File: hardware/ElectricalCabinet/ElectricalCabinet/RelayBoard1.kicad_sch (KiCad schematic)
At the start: 0 parts

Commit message: Cabinet Schematics Update
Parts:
- added C1: 0.1uF, Capacitor_SMD:C_0805_2012Metric, symbol Device:C
- added D1, D2, D3, D4, D5, D6, D7, D8: LED, LED_SMD:LED_0805_2012Metric, symbol Device:LED
- added J1: Screw_Terminal_01x09, TerminalBlock:TerminalBlock_MaiXu_MX126-5.0-09P_1x09_P5.00mm, symbol Connector:Screw_Terminal_01x09
- added J2: Screw_Terminal_01x06, TerminalBlock:TerminalBlock_MaiXu_MX126-5.0-06P_1x06_P5.00mm, symbol Connector:Screw_Terminal_01x06
- added K1, K2, K3, K4, K5, K6, K7, K8: G3MB-202P DC5, TrafficLightLibrary:G3MB_202P_DC5, symbol TrafficLightLibrary:G3MB-202P_DC5
- added R1, R2, R3, R4, R5, R6, R7, R8: 1kΩ, Resistor_SMD:R_0805_2012Metric, symbol Device:R
- added U2: TPIC6B595N, TrafficLightLibrary:TPIC6B595N, symbol TrafficLightLibrary:TPIC6B595N
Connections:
- new net: C1.1, J2.2 (Pin_2), U2.10 (GND), U2.11 (GND), U2.19 (GND), U2.9 (~{G})
- new net: J2.4 (Pin_4), U2.12 (RCK)
- new net: J2.3 (Pin_3), U2.13 (SRCK)
- new net: K5.4, R5.2, U2.14 (DRAIN4)
- new net: K6.4, R6.2, U2.15 (DRAIN5)
- new net: K7.4, R7.2, U2.16 (DRAIN6)
- new net: K8.4, R8.2, U2.17 (DRAIN7)
- new net: J2.1 (Pin_1), U2.18 (SEROUT)
- new net: C1.2, J2.6 (Pin_6), U2.2 (VCC), U2.8 (~{SRCLR})
- new net: K1.4, R1.2, U2.4 (DRAIN0)
- new net: K2.4, R2.2, U2.5 (DRAIN1)
- new net: K3.4, R3.2, U2.6 (DRAIN2)
- new net: K4.4, R4.2, U2.7 (DRAIN3)
- new net: J1.5 (Pin_5), K5.2
- new net: D1.2 (A), D2.2 (A), D3.2 (A), D4.2 (A), D5.2 (A), D6.2 (A), D7.2 (A), D8.2 (A), K1.3, K2.3, K3.3, K4.3, K5.3, K6.3, K7.3, K8.3
- new net: J1.7 (Pin_7), K7.2
- new net: J1.4 (Pin_4), K4.2
- new net: D7.1 (K), R7.1
- new net: D8.1 (K), R8.1
- new net: D6.1 (K), R6.1
- new net: J1.3 (Pin_3), K3.2
- new net: D5.1 (K), R5.1
- new net: D3.1 (K), R3.1
- new net: D4.1 (K), R4.1
- new net: D1.1 (K), R1.1
- new net: J1.1 (Pin_1), K1.2
- new net: J1.2 (Pin_2), K2.2
- new net: J1.6 (Pin_6), K6.2
- new net: J1.8 (Pin_8), K8.2
- new net: D2.1 (K), R2.1
- new net 110vAC Hawt: J1.9 (Pin_9), K1.1, K2.1, K3.1, K4.1, K5.1, K6.1, K7.1, K8.1
- new net SERIN: J2.5 (Pin_5), U2.3 (SERIN)
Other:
- note added: "110vAC Hawt"

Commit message: More updates
Added drawing sheets, wire label scheme, signal list, and traffic light label image to docs folder
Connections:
- net 110vAC Hawt: no longer names the net of J1.9 (Pin_9), K1.1, K2.1, K3.1, K4.1, K5.1, K6.1, K7.1, K8.1
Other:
- note removed: "110vAC Hawt"
- moved on the sheet: C1, D1, D2, D3, D4, D5, D6, D7, D8, K1, K2, K3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

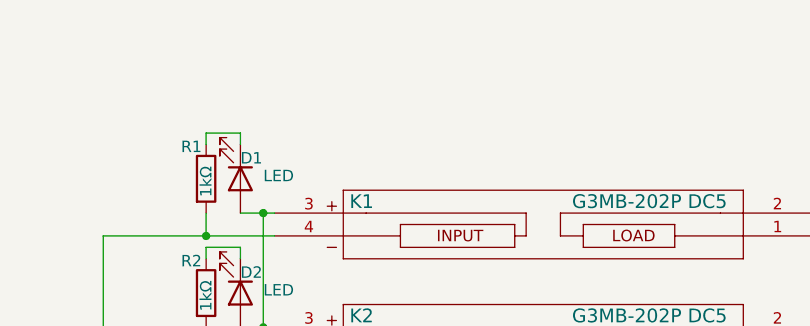
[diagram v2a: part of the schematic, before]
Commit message: Further wiring updates
Populated 6100 Bus
Corrected number of relay boards
Added 110v outputs to relay boards and noted light positon
Uploaded light scheme to documents folder
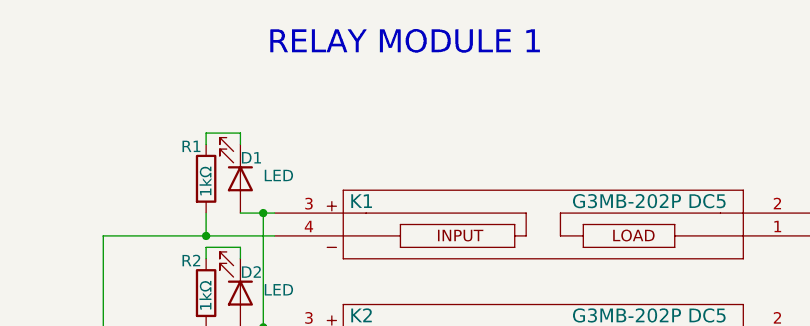
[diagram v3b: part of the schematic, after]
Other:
- note added: "RELAY MODULE 1"
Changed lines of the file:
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@@
 	(generator_version "10.0")
 	(paper "USLetter")
+	(text "RELAY MODULE 1"
+		(exclude_from_sim no)
+		(at 117.348 39.624 0)
+		(effects
+			(font
+				(size 2.54 2.54)
+			)
+		)
+	)
 	(junction
 		(at 165.1 149.86)
@@
 		(shape input)
 		(at 187.96 58.42 0)
-		(fields_autoplaced yes)
 		(effects
 			(font
@@
 			(justify left)
 		)
-		(property "Intersheetrefs" "${INTERSHEET_REFS}"
+		(property "Intersheetrefs" "LIGHTS"
 			(at 198.5651 58.42 0)
 			(hide yes)
@@
 			)
 		)
-		(property "A1" "Ref 312"
-			(at 187.96 62.2618 0)
-			(hide yes)
+		(property "REF" "A1"
+			(at 198.12 58.42 0)
 			(show_name no)
 			(do_not_autoplace no)
@@
 		(shape input)
 		(at 187.96 63.5 0)
-		(fields_autoplaced yes)
 		(effects
 			(font
@@
 			(justify left)
 		)
-		(property "Intersheetrefs" "${INTERSHEET_REFS}"
+		(property "Intersheetrefs" "LIGHTS"
 			(at 198.5651 63.5 0)
 			(hide yes)
+			(show_name no)
+			(do_not_autoplace no)
+			(effects
+				(font
+					(size 1.27 1.27)
+				)
+				(justify left)
+			)
+		)
+		(property "REF" "A3"
+			(at 198.12 63.5 0)
 			(show_name no)
 			(do_not_autoplace no)
@@
 		(shape input)
 		(at 187.96 73.66 0)
-		(fields_autoplaced yes)
 		(effects
 			(font
@@
 			(justify left)
 		)
-		(property "Intersheetrefs" "${INTERSHEET_REFS}"
+		(property "Intersheetrefs" "LIGHTS"
 			(at 198.5651 73.66 0)
 			(hide yes)
+			(show_name no)
+			(do_not_autoplace no)
+			(effects
+				(font
+					(size 1.27 1.27)
+				)
+				(justify left)
+			)
+		)
+		(property "REF" "B1"
+			(at 198.12 73.66 0)
 			(show_name no)
 			(do_not_autoplace no)
@@
 		(shape input)
 		(at 187.96 76.2 0)
-		(fields_autoplaced yes)
 		(effects
 			(font
@@
 			(justify left)
 		)
-		(property "Intersheetrefs" "${INTERSHEET_REFS}"
+		(property "Intersheetrefs" "LIGHTS"
 			(at 198.5651 76.2 0)
 			(hide yes)
+			(show_name no)
+			(do_not_autoplace no)
+			(effects
+				(font
+					(size 1.27 1.27)
+				)
+				(justify left)
+			)
+		)
+		(property "REF" "B2"
+			(at 198.12 76.2 0)
 			(show_name no)
 			(do_not_autoplace no)
@@
 		(shape input)
 		(at 187.96 66.04 0)
-		(fields_autoplaced yes)
 		(effects
 			(font
@@
 			(justify left)
 		)
-		(property "Intersheetrefs" "${INTERSHEET_REFS}"
+		(property "Intersheetrefs" "LIGHTS"
 			(at 198.5651 66.04 0)
 			(hide yes)
+			(show_name no)
+			(do_not_autoplace no)
+			(effects
+				(font
+					(size 1.27 1.27)
+				)
+				(justify left)
+			)
+		)
+		(property "REF" "A4"
+			(at 198.12 66.04 0)
 			(show_name no)
 			(do_not_autoplace no)
@@
 		(shape input)
 		(at 187.96 71.12 0)
-		(fields_autoplaced yes)
 		(effects
 			(font
@@
 			(justify left)
 		)
-		(property "Intersheetrefs" "${INTERSHEET_REFS}"
+		(property "Intersheetrefs" "LIGHTS"
 			(at 198.5651 71.12 0)
 			(hide yes)
+			(show_name no)
+			(do_not_autoplace no)
+			(effects
+				(font
+					(size 1.27 1.27)
+				)
+				(justify left)
+			)
+		)
+		(property "REF" "A6"
+			(at 198.12 71.12 0)
 			(show_name no)
 			(do_not_autoplace no)
@@
 		(shape input)
 		(at 187.96 60.96 0)
-		(fields_autoplaced yes)
 		(effects
 			(font
@@
 			(justify left)
 		)
-		(property "Intersheetrefs" "${INTERSHEET_REFS}"
+		(property "Intersheetrefs" "LIGHTS"
 			(at 198.5651 60.96 0)
 			(hide yes)
+			(show_name no)
+			(do_not_autoplace no)
+			(effects
+				(font
+					(size 1.27 1.27)
+				)
+				(justify left)
+			)
+		)
+		(property "REF" "A2"
+			(at 198.12 60.96 0)
 			(show_name no)
 			(do_not_autoplace no)
@@
 		(shape input)
 		(at 187.96 68.58 0)
-		(fields_autoplaced yes)
 		(effects
 			(font
@@
 			(justify left)
 		)
-		(property "Intersheetrefs" "${INTERSHEET_REFS}"
+		(property "Intersheetrefs" "LIGHTS"
 			(at 198.5651 68.58 0)
 			(hide yes)
+			(show_name no)
+			(do_not_autoplace no)
+			(effects
+				(font
+					(size 1.27 1.27)
+				)
+				(justify left)
+			)
+		)
+		(property "REF" "A5"
+			(at 198.12 68.58 0)
 			(show_name no)
 			(do_not_autoplace no)
@@
 			)
 		)
-		(property "Ref" "Ref 334"
+		(property "Ref" "Ref 434"
 			(at 26.67 147.32 0)
 			(show_name no)

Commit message: Electrical Cabinet done
Electrical Cabinet done, let me know if there are any changes or mistakes.
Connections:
- net SERIN is gone; now on net 7500-1: J2.5 (Pin_5), U2.3 (SERIN)
- net 5000-3: now also C1.1, J2.2 (Pin_2), U2.10 (GND), U2.11 (GND), U2.19 (GND), U2.9 (~{G})
- net 5500-3: now also C1.2, J2.6 (Pin_6), U2.2 (VCC), U2.8 (~{SRCLR})
- net 7500-2: now also J2.1 (Pin_1), U2.18 (SEROUT)
- net 8200-2: now also J2.4 (Pin_4), U2.12 (RCK)
- net 8300-2: now also J2.3 (Pin_3), U2.13 (SRCK)
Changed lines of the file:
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@@
+	)
+	(junction
+		(at 43.18 142.24)
+		(diameter 0)
+		(color 0 0 0 0)
+	)
+	(junction
+		(at 43.18 144.78)
+		(diameter 0)
+		(color 0 0 0 0)
 	)
 	(junction
@@
 	)
 	(junction
+		(at 43.18 137.16)
+		(diameter 0)
+		(color 0 0 0 0)
+	)
+	(junction
 		(at 67.31 125.73)
 		(diameter 0)
@@
 	)
 	(junction
+		(at 43.18 147.32)
+		(diameter 0)
+		(color 0 0 0 0)
+	)
+	(junction
 		(at 95.25 137.16)
 		(diameter 0)
@@
 	)
 	(junction
+		(at 43.18 139.7)
+		(diameter 0)
+		(color 0 0 0 0)
+	)
+	(junction
 		(at 101.6 147.32)
 		(diameter 0)
 		(color 0 0 0 0)
 	)
+	(junction
+		(at 43.18 134.62)
+		(diameter 0)
+		(color 0 0 0 0)
+	)
 	(wire
 		(pts
@@
 	(wire
 		(pts
+			(xy 36.83 134.62) (xy 43.18 134.62)
+		)
+		(stroke
+			(width 0)
+			(type default)
+		)
+	)
+	(wire
+		(pts
 			(xy 57.15 134.62) (xy 46.99 134.62)
 		)
@@
 	(wire
 		(pts
+			(xy 36.83 137.16) (xy 43.18 137.16)
+		)
+		(stroke
+			(width 0)
+			(type default)
+		)
+	)
+	(wire
+		(pts
 			(xy 165.1 149.86) (xy 162.56 149.86)
 		)
@@
 	(wire
 		(pts
+			(xy 36.83 147.32) (xy 43.18 147.32)
+		)
+		(stroke
+			(width 0)
+			(type default)
+		)
+	)
+	(wire
+		(pts
 			(xy 64.77 158.75) (xy 64.77 157.48)
 		)
@@
 	(wire
 		(pts
+			(xy 36.83 142.24) (xy 43.18 142.24)
+		)
+		(stroke
+			(width 0)
+			(type default)
+		)
+	)
+	(wire
+		(pts
 			(xy 99.06 121.92) (xy 101.6 121.92)
 		)
@@
 	(wire
 		(pts
+			(xy 36.83 139.7) (xy 43.18 139.7)
+		)
+		(stroke
+			(width 0)
+			(type default)
+		)
+	)
+	(wire
+		(pts
 			(xy 95.25 49.53) (xy 95.25 50.8)
 		)
@@
 		(pts
 			(xy 49.53 142.24) (xy 43.18 142.24)
+		)
+		(stroke
+			(width 0)
+			(type default)
+		)
+	)
+	(wire
+		(pts
+			(xy 36.83 144.78) (xy 43.18 144.78)
 		)
 		(stroke
@@
 		(property "Ref" "Ref 2102"
 			(at 27.94 134.62 0)
+			(hide yes)
 			(show_name no)
 			(do_not_autoplace no)
@@
 			)
 		)
-		(property "Ref" "Ref 333"
+		(property "Ref" "Ref 2002"
 			(at 18.796 144.78 0)
+			(hide yes)
 			(show_name no)
 			(do_not_autoplace no)
@@
 			)
 		)
-		(property "Ref" "Ref 332"
-			(at 26.67 139.7 0)
+		(property "Ref" "Ref 2501"
+			(at 27.686 139.7 0)
+			(hide yes)
 			(show_name no)
 			(do_not_autoplace no)
@@
 		(property "Ref" "Ref 2401"
 			(at 27.94 142.24 0)
-			(show_name no)
-			(do_not_autoplace no)
+			(hide yes)
+			(show_name no)
+			(do_not_autoplace no)
